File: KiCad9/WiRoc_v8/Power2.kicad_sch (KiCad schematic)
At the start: 21 parts, among them U15 RT8059, U16 RT8059, U17 RT8059

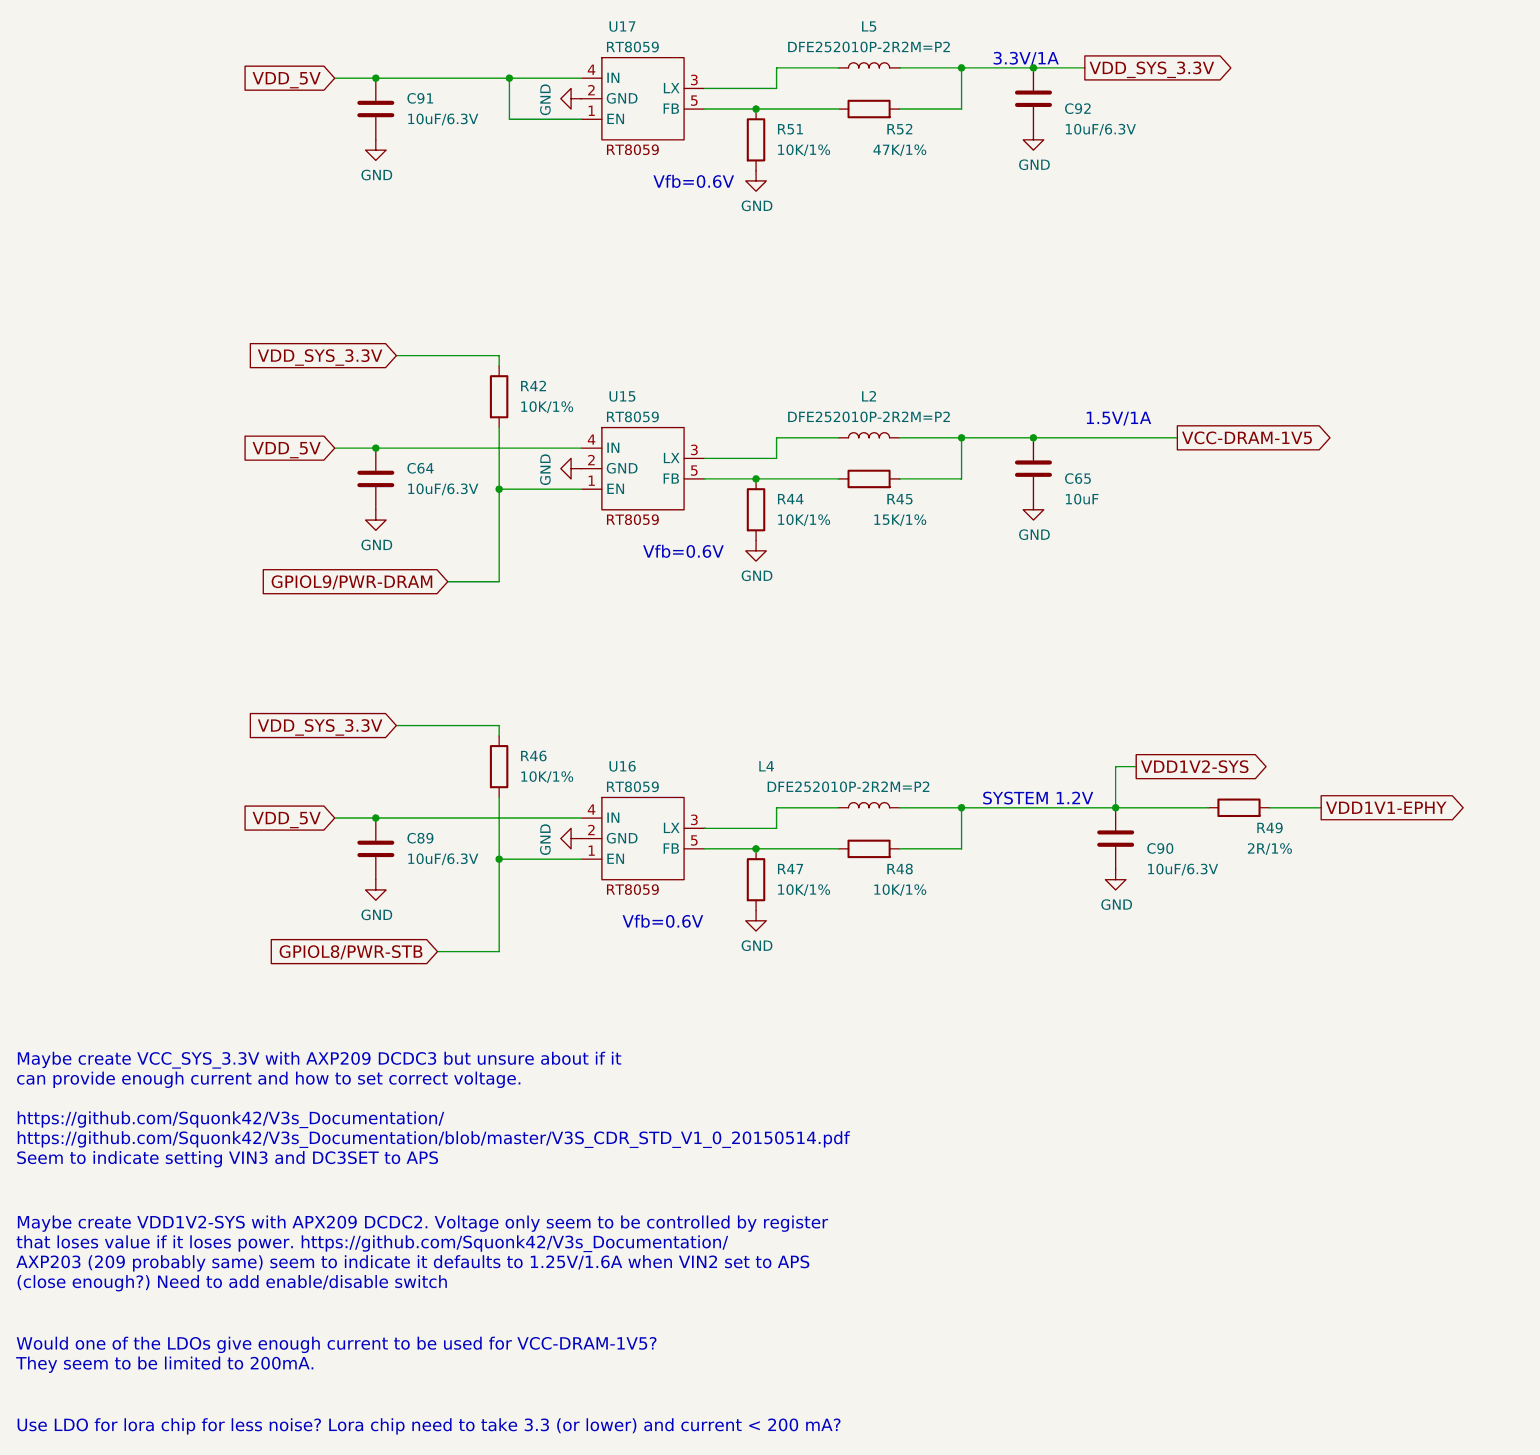
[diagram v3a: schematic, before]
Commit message: change to 10uF in pdn, vdd-dram area to south caps, remove varistor, etc
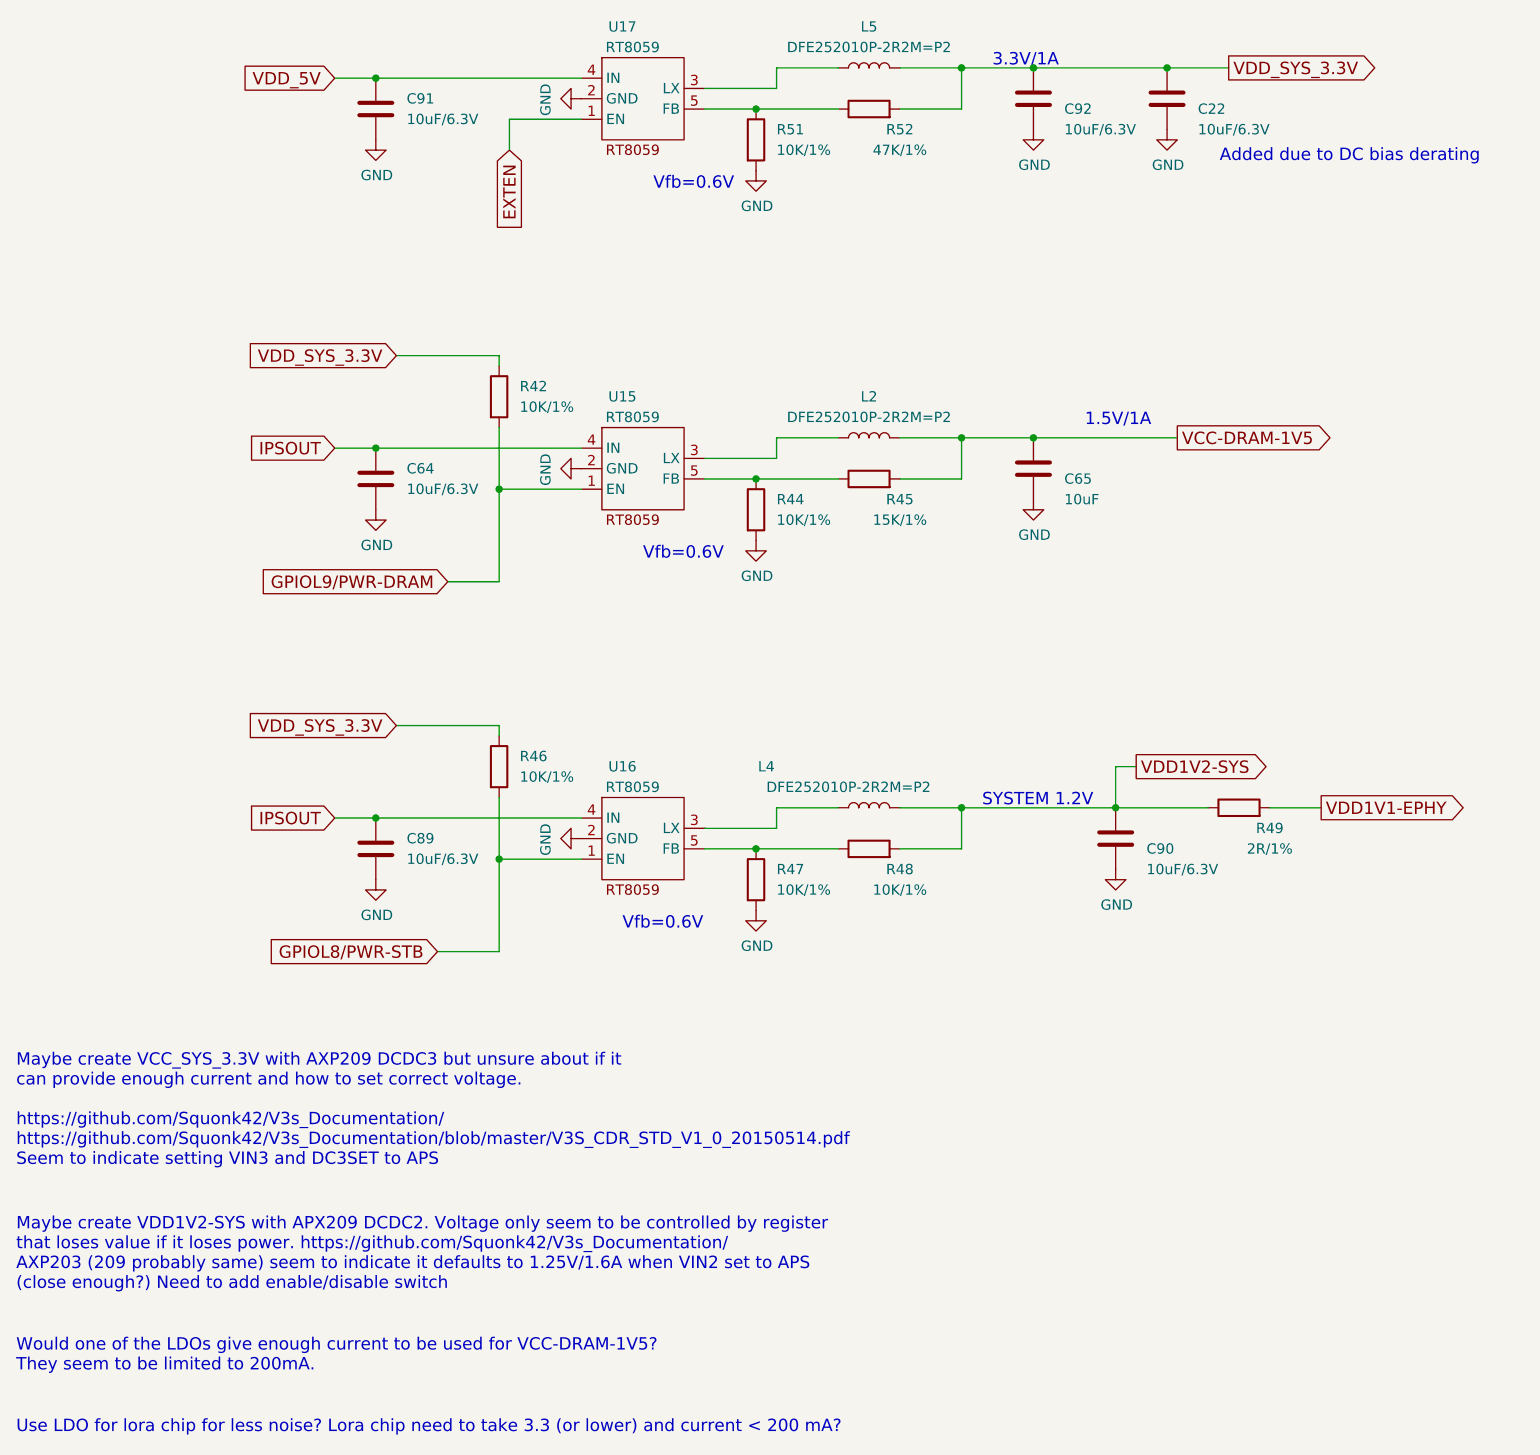
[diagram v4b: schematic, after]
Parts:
- added C22: 10uF/6.3V, Capacitor_SMD:C_0402_1005Metric, symbol Device:C
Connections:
- net GND: now also C22.2
- net VDD_5V: no longer C64.1, C89.1, U15.4 (IN), U16.4 (IN), U17.1 (EN)
- net VDD_SYS_3.3V: now also C22.1
- new net EXTEN: U17.1 (EN)
- new net IPSOUT: C64.1, C89.1, U15.4 (IN), U16.4 (IN)
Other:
- note added: "Added due to DC bias derating"
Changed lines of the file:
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@@
 		)
 	)
+	(text "Added due to DC bias derating"
+		(exclude_from_sim no)
+		(at 186.436 37.592 0)
+		(effects
+			(font
+				(size 1.524 1.524)
+			)
+		)
+	)
 	(text "Maybe create VCC_SYS_3.3V with AXP209 DCDC3 but unsure about if it\ncan provide enough current and how to set correct voltage.\n\nhttps://github.com/Squonk42/V3s_Documentation/\nhttps://github.com/Squonk42/V3s_Documentation/blob/master/V3S_CDR_STD_V1_0_20150514.pdf\nSeem to indicate setting VIN3 and DC3SET to APS"
 		(exclude_from_sim no)
@@
 	)
 	(junction
-		(at 66.04 73.66)
+		(at 163.83 26.67)
 		(diameter 0)
 		(color 0 0 0 0)
 	)
 	(junction
-		(at 147.32 72.39)
+		(at 66.04 73.66)
 		(diameter 0)
 		(color 0 0 0 0)
 	)
 	(junction
-		(at 82.55 27.94)
+		(at 147.32 72.39)
 		(diameter 0)
 		(color 0 0 0 0)
@@
 	(wire
 		(pts
+			(xy 82.55 33.02) (xy 82.55 36.83)
+		)
+		(stroke
+			(width 0)
+			(type default)
+		)
+	)
+	(wire
+		(pts
 			(xy 115.57 26.67) (xy 123.19 26.67)
 		)
@@
 	(wire
 		(pts
-			(xy 82.55 27.94) (xy 82.55 33.02)
+			(xy 176.53 118.11) (xy 182.88 118.11)
 		)
 		(stroke
@@
 	(wire
 		(pts
-			(xy 176.53 118.11) (xy 182.88 118.11)
+			(xy 81.28 90.17) (xy 74.93 90.17)
 		)
 		(stroke
@@
 	(wire
 		(pts
-			(xy 81.28 90.17) (xy 74.93 90.17)
+			(xy 113.03 123.19) (xy 123.19 123.19)
 		)
 		(stroke
@@
 	(wire
 		(pts
-			(xy 113.03 123.19) (xy 123.19 123.19)
+			(xy 163.83 26.67) (xy 171.45 26.67)
 		)
 		(stroke
@@
 	(wire
 		(pts
-			(xy 82.55 27.94) (xy 91.44 27.94)
+			(xy 66.04 27.94) (xy 91.44 27.94)
 		)
 		(stroke
@@
 	(wire
 		(pts
-			(xy 147.32 26.67) (xy 153.67 26.67)
+			(xy 147.32 26.67) (xy 163.83 26.67)
 		)
 		(stroke
@@
 	(wire
 		(pts
-			(xy 66.04 27.94) (xy 82.55 27.94)
-		)
-		(stroke
-			(width 0)
-			(type default)
-		)
-	)
-	(wire
-		(pts
 			(xy 130.81 72.39) (xy 138.43 72.39)
 		)
@@
 		)
 	)
+	(global_label "IPSOUT"
+		(shape input)
+		(at 60.96 73.66 180)
+		(fields_autoplaced yes)
+		(effects
+			(font
+				(size 1.524 1.524)
+			)
+			(justify right)
+		)
+		(property "Intersheetrefs" "${INTERSHEET_REFS}"
+			(at 50.2032 73.66 0)
+			(effects
+				(font
+					(size 1.27 1.27)
+				)
+				(justify right)
+				(hide yes)
+			)
+		)
+	)
 	(global_label "VDD1V2-SYS"
 		(shape output)
@@
 		)
 	)
-	(global_label "VDD_5V"
+	(global_label "EXTEN"
 		(shape input)
-		(at 60.96 119.38 180)
+		(at 82.55 36.83 270)
 		(fields_autoplaced yes)
 		(effects
@@
 		)
 		(property "Intersheetrefs" "${INTERSHEET_REFS}"
-			(at 49.9855 119.38 0)
+			(at 82.55 46.5937 90)
 			(effects
 				(font
@@
 		)
 	)
-	(global_label "VDD_5V"
+	(global_label "IPSOUT"
 		(shape input)
-		(at 60.96 73.66 180)
+		(at 60.96 119.38 180)
 		(fields_autoplaced yes)
 		(effects
@@
 		)
 		(property "Intersheetrefs" "${INTERSHEET_REFS}"
-			(at 49.9855 73.66 0)
+			(at 50.2032 119.38 0)
 			(effects
 				(font
@@
 	(global_label "VDD_SYS_3.3V"
 		(shape output)
-		(at 153.67 26.67 0)
+		(at 171.45 26.67 0)
 		(fields_autoplaced yes)
 		(effects
@@
 		)
 		(property "Intersheetrefs" "${INTERSHEET_REFS}"
-			(at 172.2872 26.67 0)
+			(at 190.0672 26.67 0)
 			(effects
 				(font
@@
 	)
 	(symbol
+		(lib_id "Device:C")
+		(at 163.83 30.48 0)
+		(unit 1)
+		(exclude_from_sim no)
+		(in_bom yes)
+		(on_board yes)
+		(dnp no)
+		(property "Reference" "C22"
+			(at 167.64 31.75 0)
+			(effects
+				(font
+					(size 1.27 1.27)
+				)
+				(justify left)
+			)
+		)
+		(property "Value" "10uF/6.3V"
+			(at 167.64 34.29 0)
+			(effects
+				(font
+					(size 1.27 1.27)
+				)
+				(justify left)
+			)
+		)
+		(property "Footprint" "Capacitor_SMD:C_0402_1005Metric"
+			(at 164.7952 34.29 0)
+			(effects
+				(font
+					(size 1.27 1.27)
+				)
+				(hide yes)
+			)
+		)
+		(property "Datasheet" "~"
+			(at 163.83 30.48 0)
+			(effects
+				(font
+					(size 1.27 1.27)
+				)
+				(hide yes)
+			)
+		)
+		(property "Description" ""
+			(at 163.83 30.48 0)
+			(effects
+				(font
+					(size 1.27 1.27)
+				)
+				(hide yes)
+			)
+		)
+		(property "IncludeInBOM" "TRUE"
+			(at 163.83 30.48 0)
+			(effects
+				(font
+					(size 1.27 1.27)
+				)
+				(hide yes)
+			)
+		)
+		(property "LCSC Part #" "C15525"
+			(at 163.83 30.48 0)
+			(effects
+				(font
+					(size 1.27 1.27)
+				)
+				(hide yes)
+			)
+		)
+		(property "Manufacturer" "Samsung Electro-Mechanics"
+			(at 163.83 30.48 0)
+			(effects
+				(font
+					(size 1.27 1.27)
+				)
+				(hide yes)
+			)
+		)
+		(property "ManufacturerPartNumber" "CL05A106MQ5NUNC"
+			(at 163.83 30.48 0)
+			(effects
+				(font
+					(size 1.27 1.27)
+				)
+				(hide yes)
+			)
+		)
+		(property "Package" "0402"
+			(at 163.83 30.48 0)
+			(effects
+				(font
+					(size 1.27 1.27)
+				)
+				(hide yes)
+			)
+		)
+		(property "JLCBasicExtended" "Basic"
+			(at 163.83 30.48 0)
+			(effects
+				(font
+					(size 1.27 1.27)
+				)
+				(hide yes)
+			)
+		)
+		(pin "1"
+		)
+		(pin "2"
+		)
+		(instances
+			(project "WiRoc_NanoPi"
+				(path "/8ba0b499-eaca-4cd5-a002-c6bdb610cc8c/85a0902c-c60f-4130-a6d4-27b8a234db38"
+					(reference "C22")
+					(unit 1)
+				)
+			)
+		)
+	)
+	(symbol
 		(lib_id "Device:R")
 		(at 113.03 127 0)
@@
 					(unit 1)
 				)
+			)
+		)
+	)
+	(symbol
+		(lib_id "power:GND")
+		(at 163.83 34.29 0)
+		(unit 1)
+		(exclude_from_sim no)
+		(in_bom yes)
+		(on_board yes)
+		(dnp no)
+		(property "Reference" "#PWR0115"
+			(at 163.83 40.64 0)
+			(effects
+				(font
+					(size 1.27 1.27)
+				)
+				(hide yes)
+			)
+		)
+		(property "Value" "GND"
+			(at 163.957 38.6842 0)
+			(effects
+				(font
+					(size 1.27 1.27)
+				)
+			)
+		)
+		(property "Footprint" ""
+			(at 163.83 34.29 0)
+			(effects
+				(font
+					(size 1.27 1.27)
+				)
+				(hide yes)
+			)
+		)
+		(property "Datasheet" ""
+			(at 163.83 34.29 0)
+			(effects
+				(font
+					(size 1.27 1.27)
+				)
+				(hide yes)
+			)
+		)
+		(property "Description" ""
+			(at 163.83 34.29 0)
+			(effects
+				(font
+					(size 1.27 1.27)
+				)
+				(hide yes)
+			)
+		)
+		(pin "1"
+		)
+		(instances
+			(project "WiRoc_NanoPi"
+				(path "/8ba0b499-eaca-4cd5-a002-c6bdb610cc8c/85a0902c-c60f-4130-a6d4-27b8a234db38"
+					(reference "#PWR0115")
+					(unit 1)
+				)

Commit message: many small changes, change eMMC
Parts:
- added C62: 10uF/6.3V, Capacitor_SMD:C_0402_1005Metric, symbol Device:C
- C65: value 10uF -> 10uF/6.3V
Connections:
- net GND: now also C62.2
- net VCC-DRAM-1V5: now also C62.1
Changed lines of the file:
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@@
 	)
 	(junction
+		(at 157.48 72.39)
+		(diameter 0)
+		(color 0 0 0 0)
+	)
+	(junction
 		(at 81.28 78.74)
 		(diameter 0)
@@
 	(wire
 		(pts
+			(xy 157.48 72.39) (xy 165.1 72.39)
+		)
+		(stroke
+			(width 0)
+			(type default)
+		)
+	)
+	(wire
+		(pts
 			(xy 60.96 27.94) (xy 66.04 27.94)
 		)
@@
 	(wire
 		(pts
-			(xy 147.32 72.39) (xy 165.1 72.39)
+			(xy 147.32 72.39) (xy 157.48 72.39)
 		)
 		(stroke
@@
 			)
 		)
-		(property "Value" "10uF"
+		(property "Value" "10uF/6.3V"
 			(at 151.13 80.01 0)
 			(effects
@@
 	)
 	(symbol
+		(lib_id "Device:C")
+		(at 157.48 76.2 0)
+		(unit 1)
+		(exclude_from_sim no)
+		(in_bom yes)
+		(on_board yes)
+		(dnp no)
+		(property "Reference" "C62"
+			(at 161.29 77.47 0)
+			(effects
+				(font
+					(size 1.27 1.27)
+				)
+				(justify left)
+			)
+		)
+		(property "Value" "10uF/6.3V"
+			(at 161.29 80.01 0)
+			(effects
+				(font
+					(size 1.27 1.27)
+				)
+				(justify left)
+			)
+		)
+		(property "Footprint" "Capacitor_SMD:C_0402_1005Metric"
+			(at 158.4452 80.01 0)
+			(effects
+				(font
+					(size 1.27 1.27)
+				)
+				(hide yes)
+			)
+		)
+		(property "Datasheet" "~"
+			(at 157.48 76.2 0)
+			(effects
+				(font
+					(size 1.27 1.27)
+				)
+				(hide yes)
+			)
+		)
+		(property "Description" ""
+			(at 157.48 76.2 0)
+			(effects
+				(font
+					(size 1.27 1.27)
+				)
+				(hide yes)
+			)
+		)
+		(property "LCSC Part #" "C15525"
+			(at 157.48 76.2 0)
+			(effects
+				(font
+					(size 1.27 1.27)
+				)
+				(hide yes)
+			)
+		)
+		(property "Manufacturer" "Samsung Electro-Mechanics"
+			(at 157.48 76.2 0)
+			(effects
+				(font
+					(size 1.27 1.27)
+				)
+				(hide yes)
+			)
+		)
+		(property "ManufacturerPartNumber" "CL05A106MQ5NUNC"
+			(at 157.48 76.2 0)
+			(effects
+				(font
+					(size 1.27 1.27)
+				)
+				(hide yes)
+			)
+		)
+		(property "IncludeInBOM" "TRUE"
+			(at 157.48 76.2 0)
+			(effects
+				(font
+					(size 1.27 1.27)
+				)
+				(hide yes)
+			)
+		)
+		(property "Package" "0402"
+			(at 157.48 76.2 0)
+			(effects
+				(font
+					(size 1.27 1.27)
+				)
+				(hide yes)
+			)
+		)
+		(property "JLCBasicExtended" "Basic"
+			(at 157.48 76.2 0)
+			(effects
+				(font
+					(size 1.27 1.27)
+				)
+				(hide yes)
+			)
+		)
+		(pin "1"
+		)
+		(pin "2"
+		)
+		(instances
+			(project "WiRoc_NanoPi"
+				(path "/8ba0b499-eaca-4cd5-a002-c6bdb610cc8c/85a0902c-c60f-4130-a6d4-27b8a234db38"
+					(reference "C62")
+					(unit 1)
+				)
+			)
+		)
+	)
+	(symbol
 		(lib_id "power:GND")
 		(at 147.32 34.29 0)
@@
 					(unit 1)
 				)
+			)
+		)
+	)
+	(symbol
+		(lib_id "power:GND")
+		(at 157.48 80.01 0)
+		(unit 1)
+		(exclude_from_sim no)
+		(in_bom yes)
+		(on_board yes)
+		(dnp no)
+		(property "Reference" "#PWR048"
+			(at 157.48 86.36 0)
+			(effects
+				(font
+					(size 1.27 1.27)
+				)
+				(hide yes)
+			)
+		)
+		(property "Value" "GND"
+			(at 157.607 84.4042 0)
+			(effects
+				(font
+					(size 1.27 1.27)
+				)
+			)
+		)
+		(property "Footprint" ""
+			(at 157.48 80.01 0)
+			(effects
+				(font
+					(size 1.27 1.27)
+				)
+				(hide yes)
+			)
+		)
+		(property "Datasheet" ""
+			(at 157.48 80.01 0)
+			(effects
+				(font
+					(size 1.27 1.27)
+				)
+				(hide yes)
+			)
+		)
+		(property "Description" ""
+			(at 157.48 80.01 0)
+			(effects
+				(font
+					(size 1.27 1.27)
+				)
+				(hide yes)
+			)
+		)
+		(pin "1"
+		)
+		(instances
+			(project "WiRoc_NanoPi"
+				(path "/8ba0b499-eaca-4cd5-a002-c6bdb610cc8c/85a0902c-c60f-4130-a6d4-27b8a234db38"
+					(reference "#PWR048")
+					(unit 1)
+				)
